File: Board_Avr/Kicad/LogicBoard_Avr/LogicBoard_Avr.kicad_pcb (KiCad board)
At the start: 4 copper layers, 89.2 x 87.8 mm, 46 parts, among them J1 I2C_Interface, J10 PSU Connector, J11 TriggeredStatusLedConnector, J12 PowerStatusLedConnector, J2 UART_Interface, J3 Mechanical user interface mai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, J4 Power board connector, J5 SPI Connector, J6 ICSP Header, J9 GPIO Connector, SW1 Reset switch, U1 ATmega328PB-A, U2 TLP291, U3 TLV1117-33IDCYRG3, U4 LM1117-5.0, X1 ASV-12.000MHZ-EJ-T, Y1 ABLS-20.000MHz-16-A-4-H-T

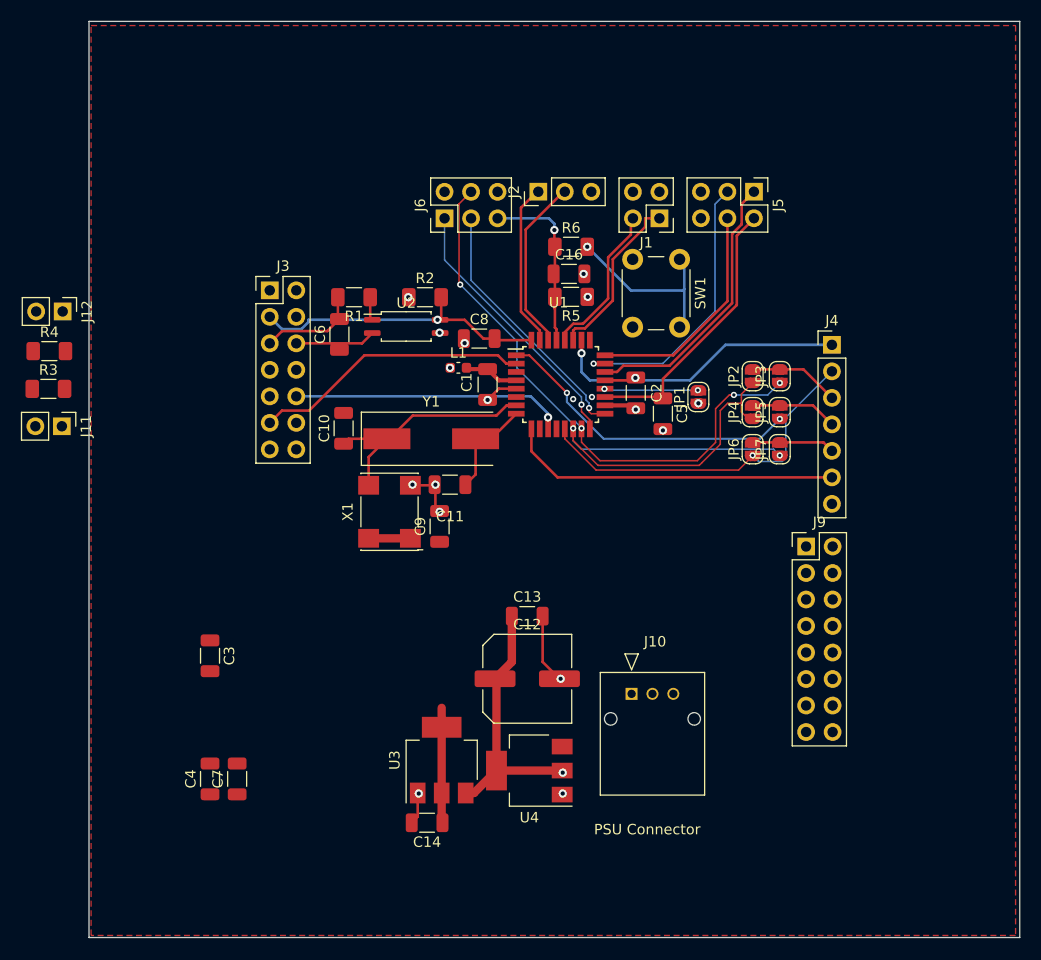
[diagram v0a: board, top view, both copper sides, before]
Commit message: Removed all microvias (unsupported by JLCPCB)
Signed-off-by: bebenlebricolo <benoittarrade@hotmail.fr>
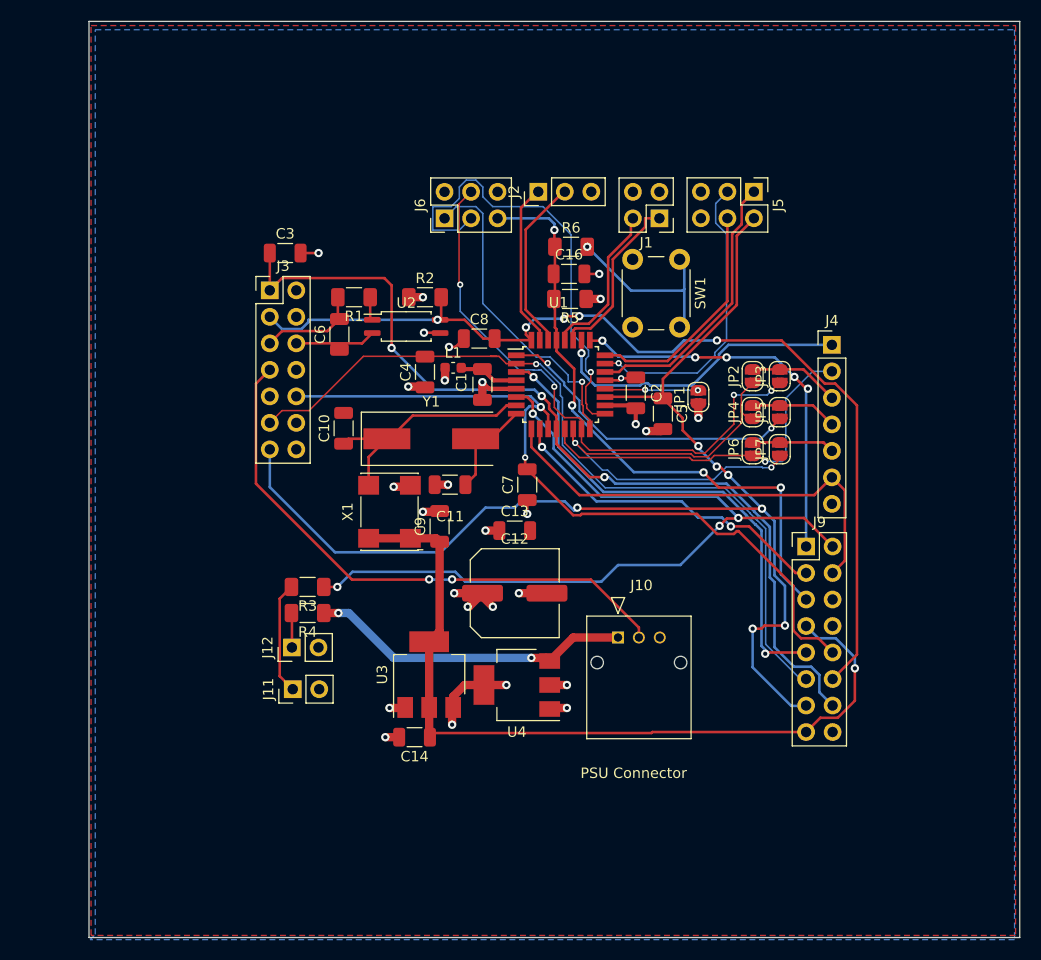
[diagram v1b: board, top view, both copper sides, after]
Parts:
- moved C4 44.1 mm to (137.0, 88.8)
- moved C7 39.6 mm to (146.8, 99.6)
- moved C3 39.3 mm to (123.6, 77.4), turned to 0 degrees
- moved J12 39.0 mm to (124.2, 115.2), turned to 90 degrees
- moved R4 35.3 mm to (125.8, 111.9), turned to 180 degrees
- moved J11 33.5 mm to (124.3, 119.2), turned to 90 degrees
- moved R3 31.3 mm to (125.8, 109.4), turned to 180 degrees
- moved C12 8.29 mm to (145.6, 110.0)
- moved C13 8.29 mm to (145.6, 104.0)
- moved C14 8.29 mm to (136.0, 123.8)
- moved U3 8.29 mm to (137.4, 117.8)
- moved U4 8.29 mm to (145.8, 118.8)
- moved J10 5.55 mm to (155.5, 114.2)
- moved C1 0.50 mm to (142.5, 90.0)
- moved L1 0.50 mm to (139.7, 88.4)
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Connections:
- R3 pad 1: /TriggeredStatusLed -> /Triggered(Out)
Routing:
- net /IntensityPot(In): track 25.7 -> 122.0 mm, vias 0 -> 7
- net /Polarity(In): track 0.00 -> 87.8 mm, vias 0 -> 3
- net /Triggered(Out): track 0.00 -> 80.9 mm, vias 0 -> 4
- net /InvertedTrigger(In): track 29.1 -> 94.4 mm, vias 1 -> 5
- net /3.3V: track 15.0 -> 78.3 mm, vias 0 -> 1
- net /PSU_Enabled: track 0.00 -> 54.9 mm, vias 0 -> 2
- net /RotEncA(In): track 26.6 -> 77.3 mm, vias 0 -> 1
- net /GPIO1: track 0.00 -> 48.6 mm, vias 0 -> 2
- net /RotEncB(In): track 26.3 -> 73.1 mm, vias 1 -> 2
- net /RESET: track 18.1 -> 60.4 mm, vias 1 -> 4
- net /OptTProbe(In): track 0.00 -> 38.4 mm, vias 0 -> 5
- net /PumpDrive(Out): track 0.00 -> 32.1 mm, vias 0 -> 2
- net /5V_PSU: track 0.00 -> 31.0 mm, vias 0 -> 2
- net /SCK0(Prog): track 24.8 -> 44.1 mm
- net /CoolingFan(Out): track 32.0 -> 43.3 mm
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- added copper zone on B.Cu, net GND

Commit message: Rerouted parts of the board and improved zones
Signed-off-by: bebenlebricolo <benoittarrade@hotmail.fr>
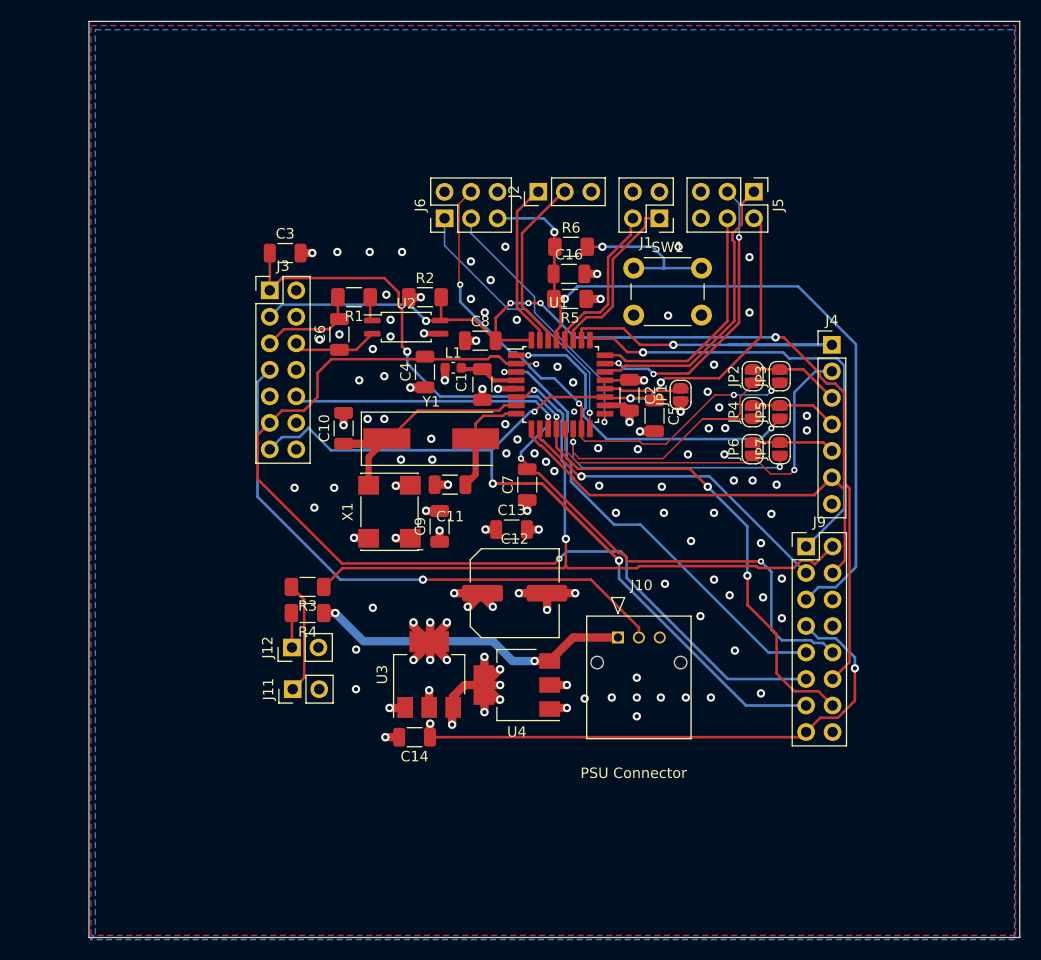
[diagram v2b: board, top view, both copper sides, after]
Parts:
- moved SW1 4.48 mm to (157.0, 78.8), turned to 0 degrees
- moved JP1 1.71 mm to (161.5, 91.0)
- moved C5 0.82 mm to (159.0, 93.0)
- moved C2 0.64 mm to (156.6, 91.0)
- moved C13 0.32 mm to (145.3, 103.9)
- moved C8 0.22 mm to (142.3, 85.8)
- moved U2 0.06 mm to (135.2, 84.5)
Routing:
- net /RotEncA(In): track 77.3 -> 99.0 mm, vias 1 -> 2
- net /SCK0(Prog): track 44.1 -> 26.2 mm
- net /RESET: track 60.4 -> 76.1 mm, vias 4 -> 2
- net /Triggered(Out): track 80.9 -> 71.5 mm, vias 4 -> 2
- net /VCC: track 28.1 -> 35.3 mm, vias 12 -> 16
- net /Ampmeter(In): track 29.6 -> 35.7 mm
- net /OptTProbe(In): track 38.4 -> 44.4 mm, vias 5 -> 1
- net /3.3V: track 78.3 -> 73.1 mm, vias 1 -> 12
- net /MISO0(Prog): track 30.9 -> 26.9 mm
- net /IntensityPot(In): track 122.0 -> 125.9 mm, vias 7 -> 5
- net /OC2A_PWM: track 55.2 -> 51.6 mm
- net /InvertedTrigger(In): track 94.4 -> 97.6 mm
- net /OC1A_PWM: track 35.3 -> 38.5 mm
- net /ResetSwitchSide: track 18.0 -> 15.4 mm
- net GND: track 31.4 -> 33.7 mm, vias 16 -> 101
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- added copper zone on In2.Cu, net /3.3V

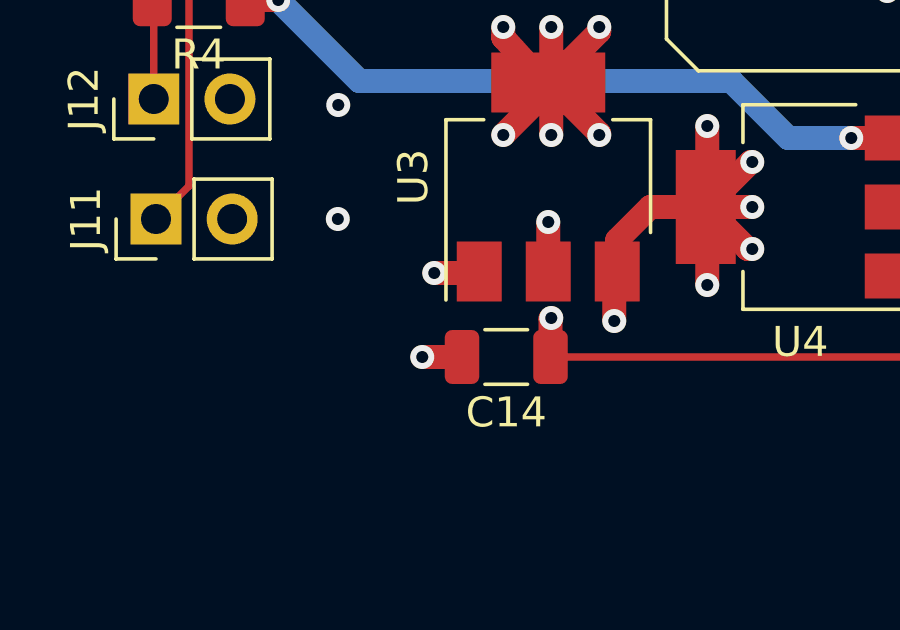
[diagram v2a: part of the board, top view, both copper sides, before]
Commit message: Updated VCC and 3.3V zones
Signed-off-by: bebenlebricolo <benoittarrade@hotmail.fr>
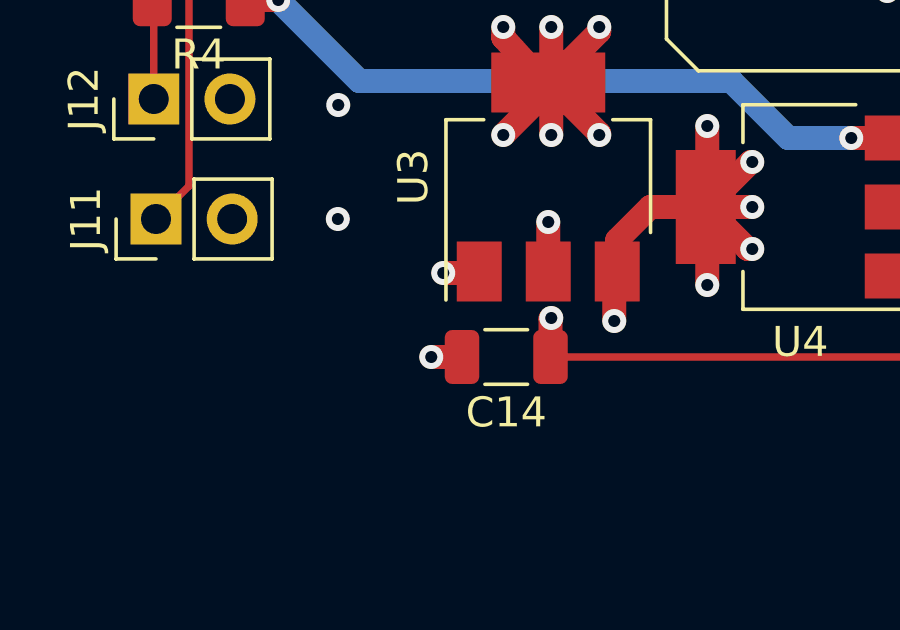
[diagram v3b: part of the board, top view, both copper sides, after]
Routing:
- net GND: track 33.7 -> 33.1 mm
- added copper zone on In2.Cu, net GND
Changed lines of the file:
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@@
   (segment (start 140.6 88.525) (end 140.475 88.4) (width 0.4) (layer "F.Cu") (net 1))
   (segment (start 150.6 121) (end 149.05 121) (width 0.8) (layer "F.Cu") (net 2))
-  (segment (start 133.6 121) (end 135.05 121) (width 0.8) (layer "F.Cu") (net 2))
+  (segment (start 133.5 123.8) (end 134.525 123.8) (width 0.8) (layer "F.Cu") (net 2))
   (segment (start 134.2 99.7) (end 135.56 99.7) (width 0.8) (layer "F.Cu") (net 2))
   (segment (start 135.56 99.7) (end 135.6 99.66) (width 0.8) (layer "F.Cu") (net 2))
@@
   (segment (start 151.4 110) (end 148.6875 110) (width 0.8) (layer "F.Cu") (net 2))
   (segment (start 138.485 85.135) (end 138.45 85.135) (width 0.25) (layer "F.Cu") (net 2))
+  (segment (start 135.05 121) (end 135.1 120.95) (width 0.8) (layer "F.Cu") (net 2))
   (segment (start 157.125 89.4) (end 157.2 89.325) (width 0.25) (layer "F.Cu") (net 2))
   (segment (start 135.625 90.275) (end 137 90.275) (width 0.8) (layer "F.Cu") (net 2))
@@
   (segment (start 136.9 85.1) (end 136.92 85.12) (width 0.6) (layer "F.Cu") (net 2))
   (segment (start 147.9 103.9) (end 146.775 103.9) (width 0.8) (layer "F.Cu") (net 2))
-  (segment (start 135.05 121) (end 135.1 120.95) (width 0.8) (layer "F.Cu") (net 2))
+  (segment (start 133.9 121) (end 135.05 121) (width 0.8) (layer "F.Cu") (net 2))
   (segment (start 139.2 99.6) (end 139.14 99.66) (width 0.8) (layer "F.Cu") (net 2))
   (segment (start 158.975 94.5) (end 159 94.475) (width 0.8) (layer "F.Cu") (net 2))
@@
   (segment (start 136.92 85.12) (end 138.5 85.12) (width 0.55) (layer "F.Cu") (net 2))
   (segment (start 146 110) (end 148.6875 110) (width 0.8) (layer "F.Cu") (net 2))
-  (segment (start 133.2 123.8) (end 134.525 123.8) (width 0.8) (layer "F.Cu") (net 2))
   (segment (start 137.1 102.1) (end 137.125 102.125) (width 0.8) (layer "F.Cu") (net 2))
   (segment (start 138.5 85.12) (end 138.485 85.135) (width 0.25) (layer "F.Cu") (net 2))
@@
   (via (at 153.6 96.1) (size 0.8) (drill 0.4) (layers "F.Cu" "B.Cu") (free) (net 2))
   (via (at 171.2 108.6) (size 0.8) (drill 0.4) (layers "F.Cu" "B.Cu") (free) (net 2))
-  (via (at 133.2 123.8) (size 0.8) (drill 0.4) (layers "F.Cu" "B.Cu") (net 2))
+  (via (at 133.5 123.8) (size 0.8) (drill 0.4) (layers "F.Cu" "B.Cu") (net 2))
   (via (at 164.7 88.1) (size 0.8) (drill 0.4) (layers "F.Cu" "B.Cu") (free) (net 2))
   (via (at 141.4 81.8) (size 0.8) (drill 0.4) (layers "F.Cu" "B.Cu") (free) (net 2))
@@
   (via (at 146 110) (size 0.8) (drill 0.4) (layers "F.Cu" "B.Cu") (net 2))
   (via (at 170.7 99.6) (size 0.8) (drill 0.4) (layers "F.Cu" "B.Cu") (free) (net 2))
-  (via (at 133.6 121) (size 0.8) (drill 0.4) (layers "F.Cu" "B.Cu") (net 2))
+  (via (at 133.9 121) (size 0.8) (drill 0.4) (layers "F.Cu" "B.Cu") (net 2))
   (via (at 133.298065 81.394197) (size 0.8) (drill 0.4) (layers "F.Cu" "B.Cu") (free) (net 2))
   (via (at 128.6 77.3) (size 0.8) (drill 0.4) (layers "F.Cu" "B.Cu") (free) (net 2))
@@
     )
   )
-  (zone (net 8) (net_name "/VCC") (layer "In2.Cu") (name "Vcc") (hatch edge 0.508)
+  (zone (net 2) (net_name "GND") (layer "In2.Cu") (name "Vcc") (hatch edge 0.508)
     (connect_pads yes (clearance 0.508))
     (min_thickness 0.254) (filled_areas_thickness no)
-    (fill yes (thermal_gap 0.508) (thermal_bridge_width 0.508))
+    (fill yes (thermal_gap 0.508) (thermal_bridge_width 0.508) (smoothing fillet) (radius 2))
     (polygon
       (pts
-        (xy 194 56.2)
-        (xy 193.2 143.4)
-        (xy 104.8 143.4)
-        (xy 105.2 55.8)
+        (xy 180.2 125.2)
+        (xy 119.2 125.2)
+        (xy 119.2 69.2)
+        (xy 180.2 69.2)
+      )
+    )
+  )
+  (zone (net 8) (net_name "/VCC") (layer "In2.Cu") (name "Vcc") (hatch edge 0.508)
+    (priority 1)
+    (connect_pads yes (clearance 0.508))
+    (min_thickness 0.254) (filled_areas_thickness no)
+    (fill yes (thermal_gap 0.508) (thermal_bridge_width 0.508) (smoothing fillet) (radius 2))
+    (polygon
+      (pts
+        (xy 159.2 69.2)
+        (xy 159.2 89.7)
+        (xy 180.2 89.700019)
+        (xy 180.2 125.2)
+        (xy 167.2 125.2)
+        (xy 167.2 111.2)
+        (xy 151.1 111.2)
+        (xy 151.1 125.2)
+        (xy 137.4 125.2)
+        (xy 137.4 102.716396)
+        (xy 119.2 102.7)
+        (xy 119.2 84.7)
+        (xy 131.7 84.7)
+        (xy 131.7 69.2)
       )
     )
   )
   (zone (net 5) (net_name "/3.3V") (layer "In2.Cu") (name "3.3V") (hatch edge 0.508)
-    (priority 1)
+    (priority 2)
     (connect_pads yes (clearance 0.508))
     (min_thickness 0.254) (filled_areas_thickness no)
@@
         (xy 140.693133 112.2)
         (xy 140.7 116.9)
-        (xy 138.5 119.1)
-        (xy 138.5 125.3)
-        (xy 136.4 125.3)
-        (xy 136.4 119.1)
+        (xy 138.9 119.1)
+        (xy 138.9 125.3)
+        (xy 135.9 125.3)
+        (xy 135.9 119.1)
         (xy 134.2 116.9)
         (xy 134.2 108.7)

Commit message: Finalised routing
Signed-off-by: bebenlebricolo <benoittarrade@hotmail.fr>
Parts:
- added R10: 33, Resistor_SMD:R_0402_1005Metric_Pad0.72x0.64mm_HandSolder, F.Cu at (154.4, 98.0)
- added R7: 33, Resistor_SMD:R_0402_1005Metric_Pad0.72x0.64mm_HandSolder, F.Cu at (154.4, 99.0)
- added R8: 33, Resistor_SMD:R_0402_1005Metric_Pad0.72x0.64mm_HandSolder, F.Cu at (154.4, 97.0)
- added R9: 33, Resistor_SMD:R_0402_1005Metric_Pad0.72x0.64mm_HandSolder, F.Cu at (154.4, 96.0)
- moved C7 1.65 mm to (145.2, 99.2), turned to 0 degrees
- moved C13 0.52 mm to (145.2, 104.4)
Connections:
- J4 pad 2: /OC1A_PWM -> /PowerBoardLink/OC1A_PWM_OUT
- JP2 pad 1: /OC1B_PWM -> /PowerBoardLink/OC1B_PWM_OUT
- JP3 pad 1: /OC2A_PWM -> /PowerBoardLink/OC2A_PWM_OUT
- JP4 pad 1: /OC1B_PWM -> /PowerBoardLink/OC1B_PWM_OUT
- JP5 pad 1: /OC2B_PWM -> /PowerBoardLink/OC2B_PWM_OUT
- JP6 pad 1: /OC1A_PWM -> /PowerBoardLink/OC1A_PWM_OUT
- JP7 pad 1: /OC1B_PWM -> /PowerBoardLink/OC1B_PWM_OUT
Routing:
- net /OC1B_PWM: track 51.4 -> 4.65 mm, vias 2 -> 0
- net /PowerBoardLink/OC1A_PWM_OUT: track 0.00 -> 33.4 mm, vias 0 -> 1
- net /OC1A_PWM: track 38.5 -> 7.10 mm, vias 1 -> 0
- net /PowerBoardLink/OC1B_PWM_OUT: track 0.00 -> 29.7 mm, vias 0 -> 3
- net /OC2A_PWM: track 51.6 -> 32.8 mm, vias 4 -> 2
- net /PowerBoardLink/OC2A_PWM_OUT: track 0.00 -> 18.6 mm
- net /RESET: track 76.1 -> 57.8 mm
- net /PowerBoardLink/OC2B_PWM_OUT: track 0.00 -> 17.9 mm
- net /OC2B_PWM: track 32.0 -> 15.6 mm
- net /3.3V: track 73.1 -> 57.2 mm, vias 12 -> 11
- net /OptTProbe(In): track 44.4 -> 33.3 mm
- net /Ampmeter(In): track 35.7 -> 25.7 mm
- net /IntensityPot(In): track 125.9 -> 117.4 mm, vias 5 -> 4
- net /RotEncA(In): track 99.0 -> 93.0 mm, vias 2 -> 1
- net /Polarity(In): track 86.9 -> 82.0 mm
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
